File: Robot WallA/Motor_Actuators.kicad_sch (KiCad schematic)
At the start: 24 parts, among them IC7 74LVC2G241DP-Q100H, J14 22-03-5035, J18 281695-3, J19 281695-3, J2 22-03-5035, J20 281695-3, J21 281695-3, J22 Conn_01x03, J23 Conn_01x03, J24 Conn_01x03, J25 Conn_01x03, J7 22-03-5035, J8 22-03-5035, Q3 BSS119, Q5 BSS119

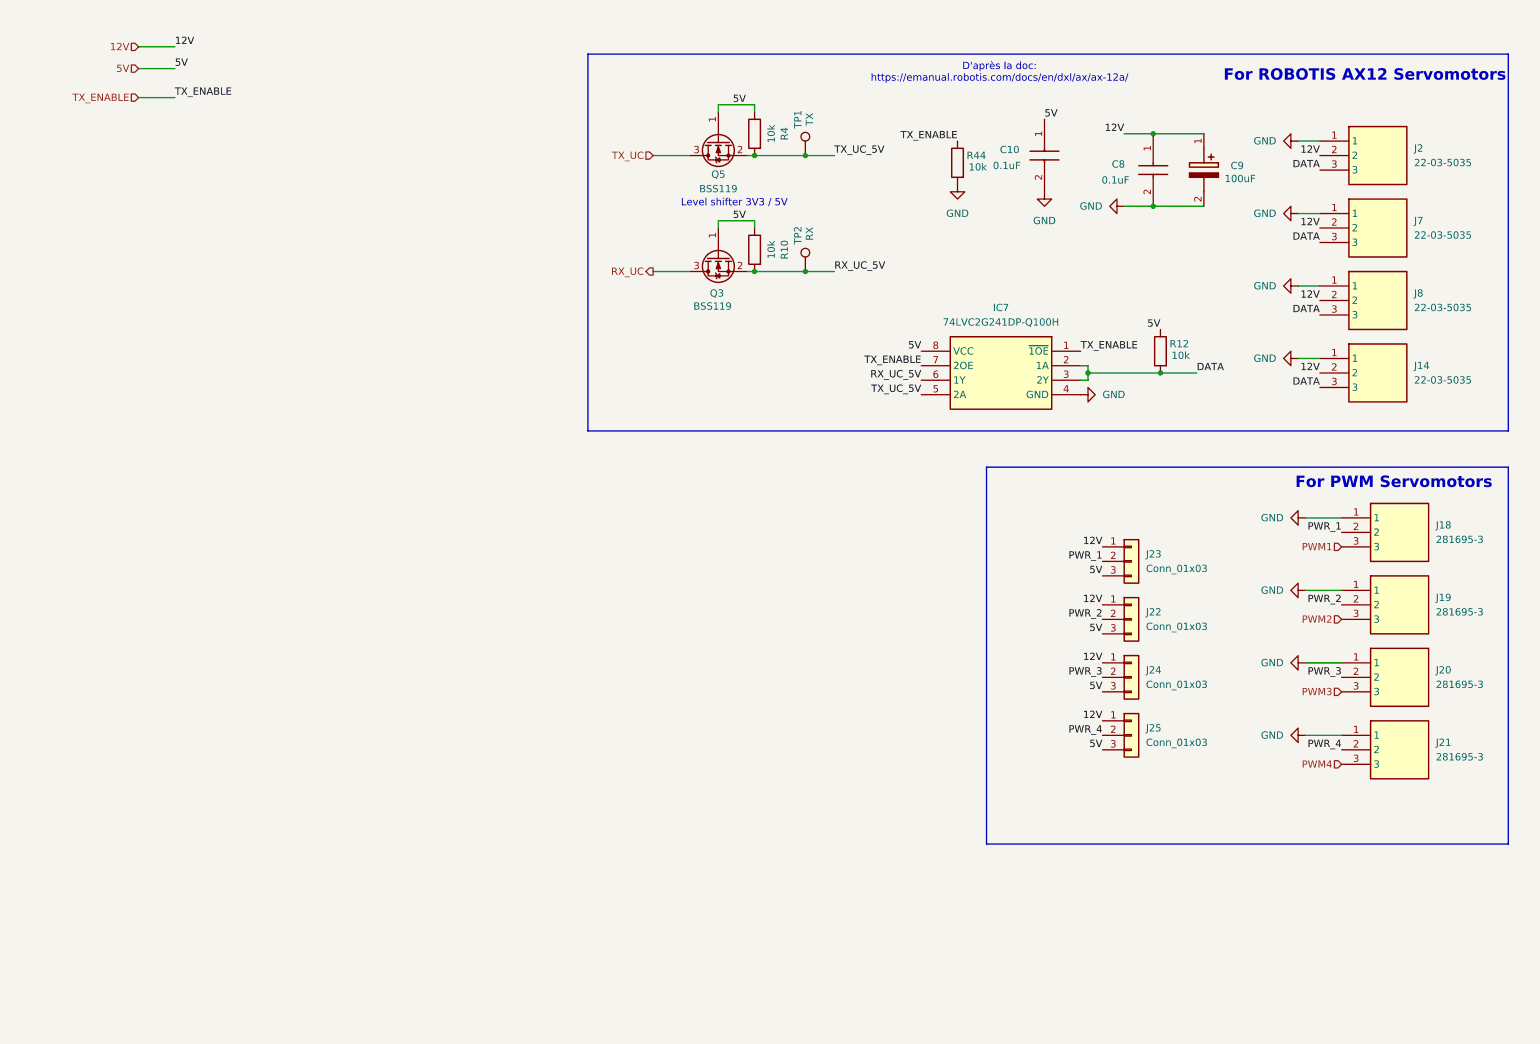
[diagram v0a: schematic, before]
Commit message: Continued to link MCU pins, Added a sheet for servomotors and optional 2 DC motors.
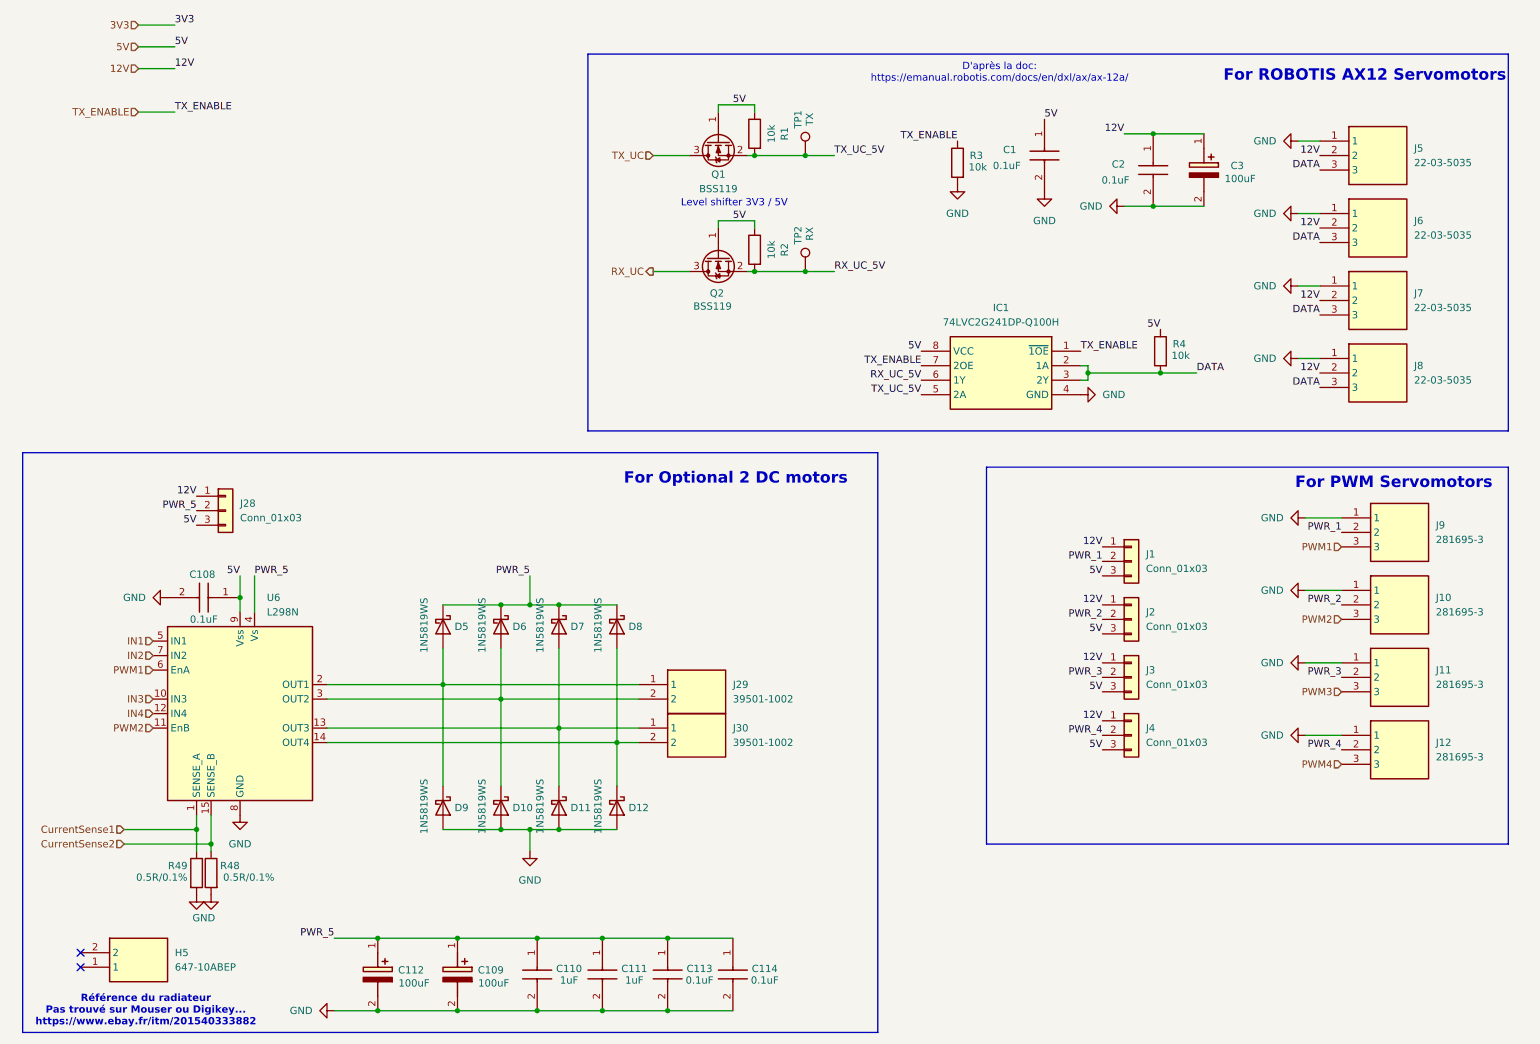
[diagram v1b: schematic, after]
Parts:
- added C108, C113, C114: 0.1uF, CAPC2012X94N, symbol SamacSys_Parts:0805DC104MAT2A
- added C109, C112: 100uF, CAPAE660X800N, symbol SamacSys_Parts:UCH1V101MCS1GS
- added C110, C111: 1uF, CAPC2012X94N, symbol SamacSys_Parts:0805DC104MAT2A
- added D10, D11, D12, D5, D6, D7, D8, D9: 1N5819WS, Diode_SMD:D_SOD-323, symbol Diode:1N5819WS
- added H5: 647-10ABEP, SamacSys_Parts:64710ABEP, symbol SamacSys_new:647-10ABEP
- added J28: Conn_01x03, Connector_PinHeader_2.54mm:PinHeader_1x03_P2.54mm_Vertical, symbol Connector_Generic:Conn_01x03
- added J29, J30: 39501-1002, 395011002, symbol SamacSys:39501-1002
- added R48, R49: 0.5R/0.1%, Resistor_SMD:R_0603_1608Metric_Pad0.98x0.95mm_HandSolder, symbol Device:R
- added U6: L298N, Package_TO_SOT_THT:TO-220-15_P2.54x5.08mm_StaggerOdd_Lead4.58mm_Vertical, symbol Driver_Motor:L298N
- renumbered C10 to C1, C8 to C2, C9 to C3, IC7 to IC1, J23 to J1, J19 to J10, J20 to J11, J21 to J12, J22 to J2, J24 to J3, J25 to J4, J2 to J5, J7 to J6, J8 to J7, J14 to J8, J18 to J9, Q5 to Q1, Q3 to Q2, R4 to R1, R10 to R2, R44 to R3, R12 to R4
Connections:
- net 12V: now also J28.1 (Pin_1)
- net 5V: now also C108.1, J28.3 (Pin_3), U6.9 (Vss)
- net GND: now also C108.2, C109.2 (-), C110.2, C111.2, C112.2 (-), C113.2, C114.2, D10.2 (A), D11.2 (A), D12.2 (A), D9.2 (A), R48.2, R49.2, U6.8 (GND)
- net PWM1: now also U6.6 (EnA)
- net PWM2: now also U6.11 (EnB)
- new net: D12.1 (K), D8.2 (A), J30.2, U6.14 (OUT4)
- new net: D11.1 (K), D7.2 (A), J30.1, U6.13 (OUT3)
- new net: D5.2 (A), D9.1 (K), J29.1, U6.2 (OUT1)
- new net: D10.1 (K), D6.2 (A), J29.2, U6.3 (OUT2)
- new net CurrentSense1: R49.1, U6.1 (SENSE_A)
- new net CurrentSense2: R48.1, U6.15 (SENSE_B)
- new net IN1: U6.5 (IN1)
- new net IN2: U6.7 (IN2)
- new net IN3: U6.10 (IN3)
- new net IN4: U6.12 (IN4)
- new net PWR_5: C109.1 (+), C110.1, C111.1, C112.1 (+), C113.1, C114.1, D5.1 (K), D6.1 (K), D7.1 (K), D8.1 (K), J28.2 (Pin_2), U6.4 (Vs)
- no-connect marks 0 -> 2
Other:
- note added: "For Optional 2 DC motors"
- note added: "Référence du radiateur Pas trouvé sur Mouser ou Digikey... https://www.ebay.fr/itm/201540333882"

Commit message: Defined every footprints
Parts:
- added JP10, JP9: SolderJumper, Jumper:SolderJumper-2_P1.3mm_Open_Pad1.0x1.5mm, symbol Jumper:SolderJumper_2_Open
- C105: renamed from C1; value 0.1uF -> 100nF; footprint CAPC2012X94N -> Capacitor_SMD:C_0603_1608Metric_Pad1.08x0.95mm_HandSolder; Arrow Part Number 0805DC104MAT2A -> (none); Arrow Price/Stock https://www.arrow.com/en/products/0805dc104mat2a/avx -> (none); Height 0.94 -> (none); Manufacturer_Name Kyocera AVX -> (none); Manufacturer_Part_Number 0805DC104MAT2A -> (none); Mouser Part Number 581-0805DC104MAT2A -> (none); Mouser Price/Stock https://www.mouser.com/Search/Refine.aspx?Keyword=581-0805D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 -> (none)
- C106: renamed from C2; value 0.1uF -> 100nF; footprint CAPC2012X94N -> Capacitor_SMD:C_0603_1608Metric_Pad1.08x0.95mm_HandSolder; Arrow Part Number 0805DC104MAT2A -> (none); Arrow Price/Stock https://www.arrow.com/en/products/0805dc104mat2a/avx -> (none); Height 0.94 -> (none); Manufacturer_Name Kyocera AVX -> (none); Manufacturer_Part_Number 0805DC104MAT2A -> (none); Mouser Part Number 581-0805DC104MAT2A -> (none); Mouser Price/Stock https://www.mouser.com/Search/Refine.aspx?Keyword=581-0805D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 -> (none)
- C107: renamed from C3; footprint CAPAE660X800N -> SamacSys_Parts:CAPAE830X1050N; Height 8 -> (none); Manufacturer_Name Nichicon -> (none); Manufacturer_Part_Number UCH1V101MCS1GS -> EDK107M050A9MAA; Mouser Part Number 647-UCH1V101MCS1GS -> (none); Mouser Price/Stock https://www.mouser.co.uk/ProductDetail/Nichicon/UCH1V101MCS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 -> (none)
- C108, C113, C114: value 0.1uF -> 100nF; footprint CAPC2012X94N -> Capacitor_SMD:C_0603_1608Metric_Pad1.08x0.95mm_HandSolder; Arrow Part Number 0805DC104MAT2A -> (none); Arrow Price/Stock https://www.arrow.com/en/products/0805dc104mat2a/avx -> (none); Height 0.94 -> (none); Manufacturer_Name Kyocera AVX -> (none); Manufacturer_Part_Number 0805DC104MAT2A -> (none); Mouser Part Number 581-0805DC104MAT2A -> (none); Mouser Price/Stock https://www.mouser.com/Search/Refine.aspx?Keyword=581-0805D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 -> (none)
- C109: renamed from C112; footprint CAPAE660X800N -> SamacSys_Parts:CAPAE830X1050N; Height 8 -> (none); Manufacturer_Name Nichicon -> (none); Manufacturer_Part_Number UCH1V101MCS1GS -> EDK107M050A9MAA; Mouser Part Number 647-UCH1V101MCS1GS -> (none); Mouser Price/Stock https://www.mouser.co.uk/ProductDetail/Nichicon/UCH1V101MCS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 -> (none)
- C110: renamed from C109; footprint CAPAE660X800N -> SamacSys_Parts:CAPAE830X1050N; Height 8 -> (none); Manufacturer_Name Nichicon -> (none); Manufacturer_Part_Number UCH1V101MCS1GS -> EDK107M050A9MAA; Mouser Part Number 647-UCH1V101MCS1GS -> (none); Mouser Price/Stock https://www.mouser.co.uk/ProductDetail/Nichicon/UCH1V101MCS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 -> (none)
- C111: renamed from C110; footprint CAPC2012X94N -> Capacitor_SMD:C_0603_1608Metric_Pad1.08x0.95mm_HandSolder; Arrow Part Number 0805DC104MAT2A -> (none); Arrow Price/Stock https://www.arrow.com/en/products/0805dc104mat2a/avx -> (none); Height 0.94 -> (none); Manufacturer_Name Kyocera AVX -> (none); Manufacturer_Part_Number 0805DC104MAT2A -> (none); Mouser Part Number 581-0805DC104MAT2A -> (none); Mouser Price/Stock https://www.mouser.com/Search/Refine.aspx?Keyword=581-0805D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 -> (none)
- C112: renamed from C111; footprint CAPC2012X94N -> Capacitor_SMD:C_0603_1608Metric_Pad1.08x0.95mm_HandSolder; Arrow Part Number 0805DC104MAT2A -> (none); Arrow Price/Stock https://www.arrow.com/en/products/0805dc104mat2a/avx -> (none); Height 0.94 -> (none); Manufacturer_Name Kyocera AVX -> (none); Manufacturer_Part_Number 0805DC104MAT2A -> (none); Mouser Part Number 581-0805DC104MAT2A -> (none); Mouser Price/Stock https://www.mouser.com/Search/Refine.aspx?Keyword=581-0805D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 -> (none)
- D10, D11, D12, D5, D6, D7, D8, D9: value 1N5819WS -> 1N5819; footprint Diode_SMD:D_SOD-323 -> Diode_SMD:D_SOD-123; Manufacturer_Part_Number (none) -> 1N5819HW-7-F
- H5: Height 25.4 -> (none); Manufacturer_Name Wakefield Thermal -> (none); Mouser Part Number 567-647-10ABEP -> (none); Mouser Price/Stock https://www.mouser.co.uk/ProductDetail/Wakefield-Thermal/64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 -> (none)
- IC9: renamed from IC1; footprint SOP65P400X110-8N -> SamacSys_Parts:SOP65P400X110-8N; Arrow Part Number 74LVC2G241DP-Q100H -> (none); Arrow Price/Stock https://www.arrow.com/en/products/74lvc2g241dp-q100h/nexper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 -> (none); Height 1.1 -> (none); Manufacturer_Name Nexperia -> (none); Mouser Part Number 771-4LVC2G241DPQ100H -> (none); Mouser Price/Stock https://www.mouser.co.uk/ProductDetail/Nexperia/74LVC2G241D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 -> (none)
- J17: renamed from J5; footprint SHDR3W60P0X250_1X3_990X490X590P -> SamacSys_Parts:SHDR3W60P0X250_1X3_990X490X590P; Height 5.9 -> (none); Manufacturer_Name Molex -> (none); Mouser Part Number 538-22-03-5035 -> (none); Mouser Price/Stock https://www.mouser.co.uk/ProductDetail/Molex/22-03-5035?qs=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 -> (none)
- J18: renamed from J6; footprint SHDR3W60P0X250_1X3_990X490X590P -> SamacSys_Parts:SHDR3W60P0X250_1X3_990X490X590P; Height 5.9 -> (none); Manufacturer_Name Molex -> (none); Mouser Part Number 538-22-03-5035 -> (none); Mouser Price/Stock https://www.mouser.co.uk/ProductDetail/Molex/22-03-5035?qs=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 -> (none)
- J19: renamed from J7; footprint SHDR3W60P0X250_1X3_990X490X590P -> SamacSys_Parts:SHDR3W60P0X250_1X3_990X490X590P; Height 5.9 -> (none); Manufacturer_Name Molex -> (none); Mouser Part Number 538-22-03-5035 -> (none); Mouser Price/Stock https://www.mouser.co.uk/ProductDetail/Molex/22-03-5035?qs=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 -> (none)
- J20: renamed from J8; footprint SHDR3W60P0X250_1X3_990X490X590P -> SamacSys_Parts:SHDR3W60P0X250_1X3_990X490X590P; Height 5.9 -> (none); Manufacturer_Name Molex -> (none); Mouser Part Number 538-22-03-5035 -> (none); Mouser Price/Stock https://www.mouser.co.uk/ProductDetail/Molex/22-03-5035?qs=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 -> (none)
- J22: renamed from J9; footprint SHDR3W65P0X254_1X3_762X508X1150P -> SamacSys_Parts:SHDR3W65P0X254_1X3_762X508X1150P; Arrow Part Number 281695-3 -> (none); Arrow Price/Stock https://www.arrow.com/en/products/281695-3/te-connectivity?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 -> (none); Height 11.5 -> (none); Manufacturer_Name TE Connectivity -> (none); Mouser Part Number 571-281695-3 -> (none); Mouser Price/Stock https://www.mouser.co.uk/ProductDetail/TE-Connectivity/2816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 -> (none)
- J24: renamed from J10; footprint SHDR3W65P0X254_1X3_762X508X1150P -> SamacSys_Parts:SHDR3W65P0X254_1X3_762X508X1150P; Arrow Part Number 281695-3 -> (none); Arrow Price/Stock https://www.arrow.com/en/products/281695-3/te-connectivity?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 -> (none); Height 11.5 -> (none); Manufacturer_Name TE Connectivity -> (none); Mouser Part Number 571-281695-3 -> (none); Mouser Price/Stock https://www.mouser.co.uk/ProductDetail/TE-Connectivity/2816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 -> (none)
- J26: renamed from J11; footprint SHDR3W65P0X254_1X3_762X508X1150P -> SamacSys_Parts:SHDR3W65P0X254_1X3_762X508X1150P; Arrow Part Number 281695-3 -> (none); Arrow Price/Stock https://www.arrow.com/en/products/281695-3/te-connectivity?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 -> (none); Height 11.5 -> (none); Manufacturer_Name TE Connectivity -> (none); Mouser Part Number 571-281695-3 -> (none); Mouser Price/Stock https://www.mouser.co.uk/ProductDetail/TE-Connectivity/2816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 -> (none)
- J28: renamed from J29; footprint 395011002 -> SamacSys_Parts:395011002; Height 9.6 -> (none); Manufacturer_Name Molex -> (none); Mouser Part Number 538-39501-1002 -> (none); Mouser Price/Stock https://www.mouser.co.uk/ProductDetail/Molex/39501-1002?qs=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 -> (none)
- J29: renamed from J30; footprint 395011002 -> SamacSys_Parts:395011002; Height 9.6 -> (none); Manufacturer_Name Molex -> (none); Mouser Part Number 538-39501-1002 -> (none); Mouser Price/Stock https://www.mouser.co.uk/ProductDetail/Molex/39501-1002?qs=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 -> (none)
- J31: renamed from J12; footprint SHDR3W65P0X254_1X3_762X508X1150P -> SamacSys_Parts:SHDR3W65P0X254_1X3_762X508X1150P; Arrow Part Number 281695-3 -> (none); Arrow Price/Stock https://www.arrow.com/en/products/281695-3/te-connectivity?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 -> (none); Height 11.5 -> (none); Manufacturer_Name TE Connectivity -> (none); Mouser Part Number 571-281695-3 -> (none); Mouser Price/Stock https://www.mouser.co.uk/ProductDetail/TE-Connectivity/2816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 -> (none)
- Q4: renamed from Q1; footprint SOT95P260X110-3N -> SamacSys_Parts:SOT95P260X110-3N; Arrow Part Number BSS119NH6327XTSA1 -> (none); Arrow Price/Stock https://www.arrow.com/en/products/bss119nh6327xtsa1/infineo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 -> (none); Height 1.1 -> (none); Manufacturer_Name Infineon -> (none); Mouser Part Number 726-BSS119NH6327XTSA -> (none); Mouser Price/Stock https://www.mouser.co.uk/ProductDetail/Infineon-Technologie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 -> (none); Mouser Reference 726-BSS119NH6327XTSA -> (none)
- Q5: renamed from Q2; footprint SOT95P260X110-3N -> SamacSys_Parts:SOT95P260X110-3N; Arrow Part Number BSS119NH6327XTSA1 -> (none); Arrow Price/Stock https://www.arrow.com/en/products/bss119nh6327xtsa1/infineo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 -> (none); Height 1.1 -> (none); Manufacturer_Name Infineon -> (none); Mouser Part Number 726-BSS119NH6327XTSA -> (none); Mouser Price/Stock https://www.mouser.co.uk/ProductDetail/Infineon-Technologie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 -> (none); Mouser Reference 726-BSS119NH6327XTSA -> (none)
- R44: renamed from R1; Manufacturer_Part_Number ERJ-3GEYJ103V -> (none); Mouser Reference 667-ERJ-3GEYJ103V -> (none)
- R45: renamed from R3; Manufacturer_Part_Number ERJ-3GEYJ103V -> (none); Mouser Reference 667-ERJ-3GEYJ103V -> (none)
- R46: renamed from R2; Manufacturer_Part_Number ERJ-3GEYJ103V -> (none); Mouser Reference 667-ERJ-3GEYJ103V -> (none)
- R47: renamed from R4; Manufacturer_Part_Number ERJ-3GEYJ103V -> (none); Mouser Reference 667-ERJ-3GEYJ103V -> (none)
- R48: renamed from R49; Manufacturer_Part_Number ERJ-3GEYJ103V -> (none); Mouser Reference 667-ERJ-3GEYJ103V -> (none)
- R49: renamed from R48; Manufacturer_Part_Number ERJ-3GEYJ103V -> (none); Mouser Reference 667-ERJ-3GEYJ103V -> (none)
- TP1, TP2: Manufacturer_Part_Number NC -> (none); Mouser Reference NC -> (none); RS Reference NC -> (none)
- renumbered J28 to J21, J1 to J23, J2 to J25, J3 to J27, J4 to J30
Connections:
- net CurrentSense1: now also JP9.1 (A); no longer R48.1, U6.1 (SENSE_A)
- net CurrentSense2: now also JP10.1 (A); no longer R49.1, U6.15 (SENSE_B)
- net DATA: now also J17.1, J18.1, J19.1, J20.1; no longer J17.3, J18.3, J19.3, J20.3
- net GND: now also J17.3, J18.3, J19.3, J20.3; no longer J17.1, J18.1, J19.1, J20.1
- net PWM1: no longer U6.6 (EnA)
- net PWM2: no longer U6.11 (EnB)
- new net: JP10.2 (B), R49.1, U6.15 (SENSE_B)
- new net: JP9.2 (B), R48.1, U6.1 (SENSE_A)
- new net PWM5: U6.6 (EnA)
- new net PWM6: U6.11 (EnB)
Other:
- moved on the sheet: R48, R49

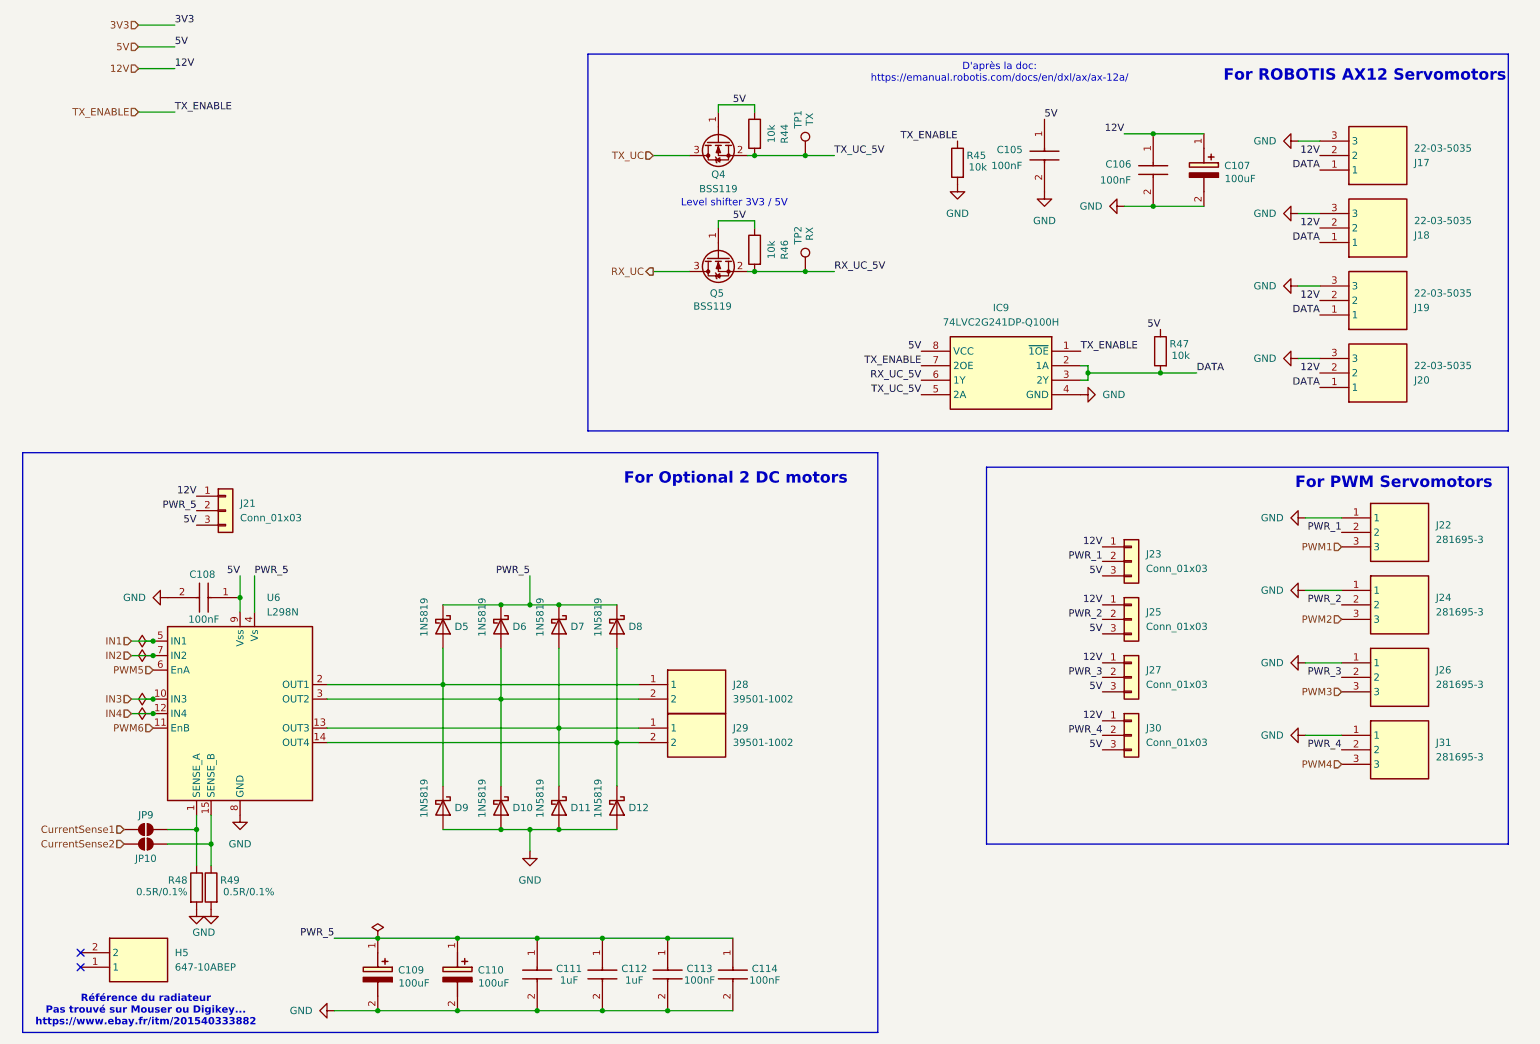
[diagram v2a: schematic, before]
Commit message: Updated USB UART converter, Linked telemeter sensors.
Updated components indicators
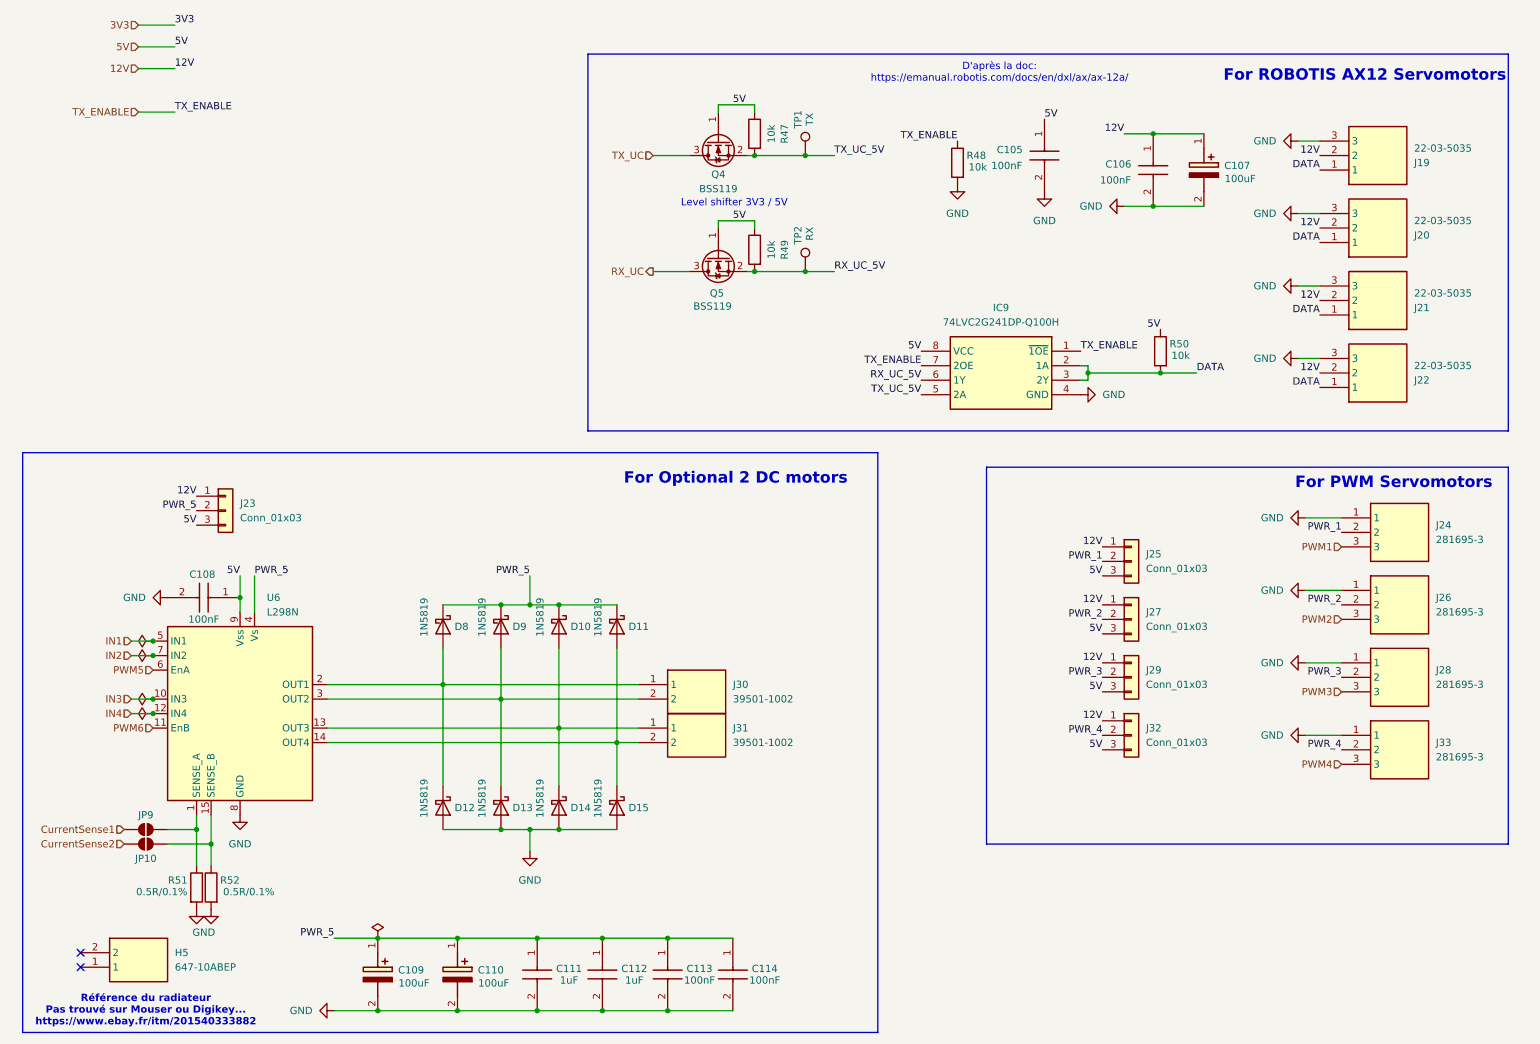
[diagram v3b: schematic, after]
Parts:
- U6: Manufacturer_Part_Number (none) -> L298N
- renumbered D7 to D10, D8 to D11, D9 to D12, D10 to D13, D11 to D14, D12 to D15, D5 to D8, D6 to D9, J17 to J19, J18 to J20, J19 to J21, J20 to J22, J21 to J23, J22 to J24, J23 to J25, J24 to J26, J25 to J27, J26 to J28, J27 to J29, J28 to J30, J29 to J31, J30 to J32, J31 to J33, R44 to R47, R45 to R48, R46 to R49, R47 to R50, R48 to R51, R49 to R52

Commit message: Continue to route
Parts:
- added R26: 0R, Resistor_SMD:R_0603_1608Metric_Pad0.98x0.95mm_HandSolder, symbol Device:R
- TP1, TP2: footprint TestPoint:TestPoint_Pad_D2.0mm -> TestPoint:TestPoint_Pad_D1.0mm
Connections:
- net 5V: now also R26.1; no longer C105.1, IC9.8 (VCC), Q4.1, Q5.1, R47.1, R49.1, R50.1
- net GND: now also H5.1, H5.2
- net Motor2_Low: now reaches D11.2 (A), D15.1 (K), J31.2, U6.14 (OUT4)
- net Motor2_High: now reaches D10.2 (A), D14.1 (K), J31.1, U6.13 (OUT3)
- net Motor1_High: now reaches D12.1 (K), D8.2 (A), J30.1, U6.2 (OUT1)
- net Motor1_Low: now reaches D13.1 (K), D9.2 (A), J30.2, U6.3 (OUT2)
- new net 5V_ROBOTIS: C105.1, IC9.8 (VCC), Q4.1, Q5.1, R26.2, R47.1, R49.1, R50.1
- no-connect marks 2 -> 0

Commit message: continue
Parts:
- removed C107: 100uF, SamacSys_Parts:CAPAE830X1050N, symbol SamacSys_Parts:UCH1V101MCS1GS
- added C107, C130, C131: 10uF, Capacitor_SMD:C_0603_1608Metric_Pad1.08x0.95mm_HandSolder, symbol SamacSys_Parts:0805DC104MAT2A
- C106: value 100nF -> 10uF
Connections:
- net 12V: now also C107.1, C130.1, C131.1
- net GND: now also C107.2, C130.2, C131.2
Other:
- moved on the sheet: C105, R48
